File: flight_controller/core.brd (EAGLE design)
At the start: 94 x 90 mm, 116 parts, among them J1 MOLEX-2POS, J10 MOLEX-2POS, J11 MOLEX-2POS, J12 MOLEX-2POS, J13 MOLEX-3POS, J14 MOLEX-3POS, J15 MOLEX-4POS, J16 MOLEX-3POS, J17 MOLEX-3POS, J18 MOLEX-4POS, J19 MOLEX-3POS, J2 MOLEX-2POS, J20 MOLEX-4POS, J3 MOLEX-2POS, J4 MOLEX-2POS, J5 MOLEX-2POS, J6 MOLEX-2POS, J7 MOLEX-2POS, J8 MOLEX-2POS, J9 MOLEX-2POS, Q1 MMBT2222A, Q14 MMBT2222A, Q15 MMBT2222A, Q16 MMBT2222A, Q17 MMBT2222A, Q3 MMBT2222A, Q4 MMBT2222A, Q9 MMBT2222A, U1 MPU-6000QFN-24, U2 MEAS-MS5611, U3 USD-SOCKETNEW, U4 STM32F405, U5 MIC5219 3.3V

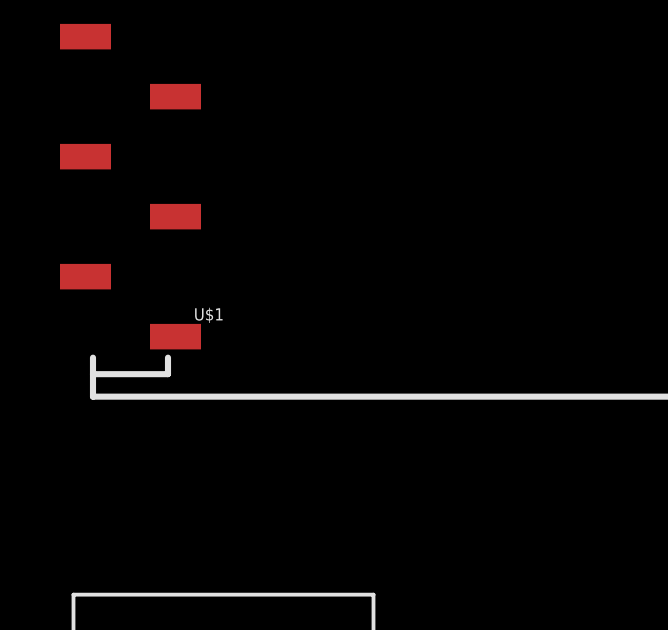
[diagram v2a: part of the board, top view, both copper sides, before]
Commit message: Explicitly name XBee package.
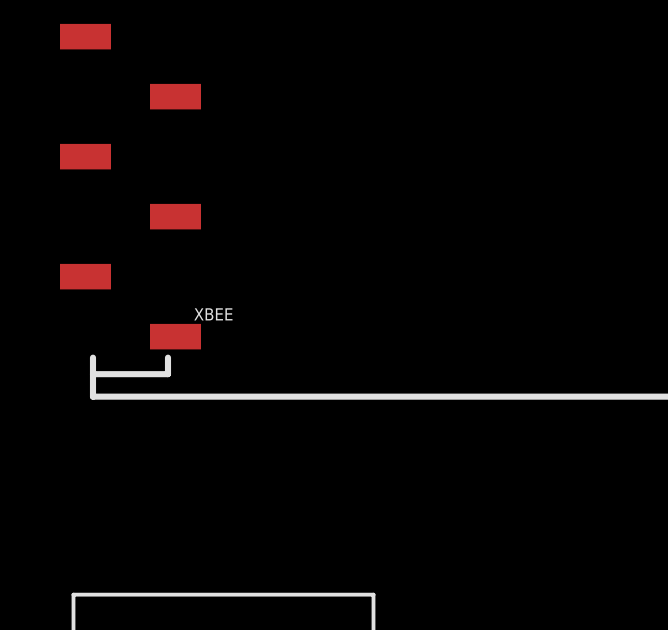
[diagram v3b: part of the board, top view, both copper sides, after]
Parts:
- renumbered U$1 to XBEE
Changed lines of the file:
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@@
 <attribute name="PROD_ID" value="CAP-08267" x="-187.5" y="-506.7" size="1.778" layer="27" display="off"/>
 </element>
-<element name="U$1" library="SparkFun-RF" package="XBEE-SMD" value="XBEE-1B3" x="-202.6" y="-501.9">
+<element name="XBEE" library="SparkFun-RF" package="XBEE-SMD" value="XBEE-1B3" x="-202.6" y="-501.9">
 <attribute name="PROD_ID" value="CONN-09042" x="-202.6" y="-501.9" size="1.778" layer="27" display="off"/>
 </element>
@@
 <contactref element="C15" pad="2"/>
 <contactref element="C16" pad="2"/>
-<contactref element="U$1" pad="10"/>
+<contactref element="XBEE" pad="10"/>
 <contactref element="J18" pad="4"/>
 <contactref element="R13" pad="1"/>
@@
 <contactref element="R8" pad="1"/>
 <contactref element="J20" pad="1"/>
-<contactref element="U$1" pad="5"/>
+<contactref element="XBEE" pad="5"/>
 <contactref element="U4" pad="7"/>
 <wire x1="-11.4" y1="-155.2" x2="-14.15" y2="-182.7" width="0" layer="19" extent="1-1"/>
@@
 <contactref element="U4" pad="64"/>
 <contactref element="C9" pad="1"/>
-<contactref element="U$1" pad="1"/>
+<contactref element="XBEE" pad="1"/>
 <wire x1="-138" y1="-372.6" x2="-129.4" y2="-372.6" width="0" layer="19" extent="1-1"/>
 <wire x1="-180.7138" y1="-413.9967" x2="-138" y2="-372.6" width="0" layer="19" extent="1-1"/>
@@
 <contactref element="R11" pad="1"/>
 <contactref element="R13" pad="2"/>
-<contactref element="U$1" pad="20"/>
+<contactref element="XBEE" pad="20"/>
 <wire x1="-184.75" y1="-435.8" x2="-27.55" y2="-219.5" width="0" layer="19" extent="1-1"/>
 <wire x1="-183.05" y1="-438.8" x2="-184.75" y2="-435.8" width="0" layer="19" extent="1-1"/>
@@
 <signal name="RSSI">
 <contactref element="R27" pad="1"/>
-<contactref element="U$1" pad="6"/>
+<contactref element="XBEE" pad="6"/>
 <wire x1="-212.1" y1="-491.9" x2="-30.65" y2="-219.5" width="0" layer="19" extent="1-1"/>
 </signal>
@@
 <signal name="UART2-TX-XBEE">
 <contactref element="U4" pad="16"/>
-<contactref element="U$1" pad="3"/>
+<contactref element="XBEE" pad="3"/>
 <contactref element="J17" pad="1"/>
 <contactref element="R29" pad="1"/>
@@
 <signal name="UART2-RX-XBEE">
 <contactref element="U4" pad="17"/>
-<contactref element="U$1" pad="2"/>
+<contactref element="XBEE" pad="2"/>
 <contactref element="J17" pad="2"/>
 <contactref element="R30" pad="1"/>

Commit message: Remove XBee reset pin from global reset net.
The XBee pin is for factory resetting the device! Read the datasheet, people!
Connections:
- net RST: no longer XBEE.5
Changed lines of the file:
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@@
 <contactref element="R8" pad="1"/>
 <contactref element="J20" pad="1"/>
-<contactref element="XBEE" pad="5"/>
 <contactref element="U4" pad="7"/>
 <wire x1="-11.4" y1="-155.2" x2="-14.15" y2="-182.7" width="0" layer="19" extent="1-1"/>
 <wire x1="-42.794" y1="-359.895" x2="-14.15" y2="-182.7" width="0" layer="19" extent="1-1"/>
 <wire x1="-183" y1="-382.5" x2="-42.794" y2="-359.895" width="0" layer="19" extent="1-1"/>
-<wire x1="-215.1" y1="-489.9" x2="-183" y2="-382.5" width="0" layer="19" extent="1-1"/>
 </signal>
 <signal name="PA12">

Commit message: Add RGB status LED pair.
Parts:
- removed J10, J11, J12: MOLEX-2POS, aerial:MOLEX-2MM-MICROLATCH-2POS-RA
- removed LED16, LED17, LED18, LED19, LED20, LED21: GREEN, SparkFun-LED:LED-0603
- removed R35, R36: 680, SparkFun-Passives:0603-RES
- added Q2, Q5, Q6: 200mA/50V, SparkFun-DiscreteSemi:SOT23-3
- LED14, LED15: value GREEN -> OSRAM-MULTILED-RGB; device SparkFun-LED:LED-0603 -> aerial:PLCC-6
- R10, R26: value 680 -> 120
- R24, R25, R33, R34: value 680 -> 100
- moved R34 388.2 mm to (-223.8, -555.1)
- moved R33 384.0 mm to (-223.8, -552.1)
- moved R24 383.1 mm to (-223.8, -543.1)
- moved R26 380.9 mm to (-223.8, -549.1)
- moved R25 376.7 mm to (-223.8, -546.1)
- moved LED15 376.2 mm to (-222.5, -537.0)
- moved LED5 365.7 mm to (-214.8, -519.7)
- moved LED6 365.7 mm to (-211.9, -519.7)
- moved LED14 365.1 mm to (-213.3, -531.3)
- moved LED7 359.8 mm to (-214.8, -522.8)
- moved R10 247.7 mm to (-223.8, -540.1)
- moved R4 233.2 mm to (-214.5, -525.7)
- moved R3 226.7 mm to (-211.6, -522.6)
- moved R7 226.6 mm to (-211.4, -525.7)
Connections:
- net TIM3-CH1-K renamed TIM4-CH1-K
- net TIM3-CH2-K renamed TIM4-CH2-K
- net TIM3-CH3-K renamed TIM4-CH3-K
- net TIM3-CH4-K renamed TIM4-CH4-K
- removed net N$31: LED5.A, R24.2
- removed net N$32: LED6.A, R25.2
- removed net N$33: LED7.A, R26.2
- removed net N$40: LED14.A, R33.2
- removed net N$41: LED15.A, R34.2
- removed net N$42: LED16.A, R35.2
- removed net N$43: LED17.A, R36.2
- removed net RSSI: R27.1, XBEE.6
- removed net TIM3-CH2: R10.1, R40.1, U4.23
- removed net TIM3-CH3: R3.1, R41.1, U4.26
- removed net TIM3-CH4: R4.1, R42.1, U4.27
- new net N$12: LED14.A1, R25.2
- new net N$19: LED15.A1, R34.2
- new net N$3: LED6.A, R4.2
- new net N$5: LED14.C1, LED15.C1, Q2.3
- new net N$6: LED14.C3, LED15.C3, Q5.3
- new net N$7: LED14.C2, LED15.C2, Q6.3
- new net N$8: LED14.A2, R10.2
- new net N$9: LED14.A3, R24.2
- new net TIM3-CH1-RSSI: R27.1, U4.22, XBEE.6
- new net TIM3-CH2-STSB: Q2.1
- new net TIM3-CH2-STSR: U4.23
- new net TIM3-CH3-STSG: Q5.1, U4.26
- new net TIM3-CH4-STSB: U4.27
- new net TIM3-CH4-STSR: Q6.1
- net 5V: now also R10.1, R24.1, R25.1, R26.1, R33.1, R34.1
- net GND: now also Q2.2, Q5.2, Q6.2; no longer J10.2, J11.2, J12.2, LED14.C, LED15.C, LED16.C, LED17.C, LED18.C, LED19.C, LED20.C, LED21.C
- net N$15: now also LED15.A2, R26.2; no longer LED20.A, R7.2
- net N$16: now also LED15.A3, R33.2; no longer LED21.A, R10.2
- net N$2: now also LED5.A; no longer LED18.A
- net N$4: now also LED7.A, R7.2; no longer LED19.A, R4.2
- net PA12: now also R3.1; no longer R25.1
- net PA15: now also R4.1; no longer R26.1
- net PB2: now also R7.1; no longer R24.1
- net TIM1-CH1: no longer R35.1
- net TIM1-CH2: no longer R36.1
- net TIM1-CH3: no longer R33.1
- net TIM1-CH4: no longer R34.1
- net TIM3-CH1: now also J9.1; no longer R39.1, R7.1, U4.22
- net TIM4-CH1: now also R39.1; no longer J9.1
- net TIM4-CH2: now also R40.1; no longer J10.1
- net TIM4-CH3: now also R41.1; no longer J11.1
- net TIM4-CH4: now also R42.1; no longer J12.1

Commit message: Replace components to those from new OSURC libraries.
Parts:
- J1: device aerial:MOLEX-2MM-MICROLATCH-2POS-RA -> OSURC_Connectors:MOLEX-2MM-MICROLATCH-2POS-RA
- J17: device aerial:MOLEX-2MM-MICROLATCH-3POS-RA -> OSURC_Connectors:MOLEX-2MM-MICROLATCH-3POS-RA
- J18: device aerial:MOLEX-2MM-MICROLATCH-4POS-RA -> OSURC_Connectors:MOLEX-2MM-MICROLATCH-4POS-RA
- LED14: device aerial:PLCC-6 -> OSURC_LED:PLCC-6
- U2: device aerial:MEAS-MS5611 -> OSURC_Sensors:MEAS-MS5611
- U4: device aerial:LQFP-64-STM32F405 -> OSURC_DigitalIC:LQFP-64-STM32F405
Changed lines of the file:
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@@
 <attribute name="PROD_ID" value="CONN-07820" x="-0.5" y="-145.6" size="1.778" layer="27" display="off"/>
 </element>
-<element name="U4" library="aerial" package="LQFP-64-STM32F405" value="STM32F405" x="-11.8" y="-162.3"/>
+<element name="U4" library="OSURC_DigitalIC" package="LQFP-64-STM32F405" value="STM32F405" x="-11.8" y="-162.3"/>
 <element name="R8" library="SparkFun" package="0603-RES" value="20K" x="-13.3" y="-182.7"/>
 <element name="C8" library="SparkFun-Capacitors" package="0603-CAP" value="0.1uF" x="-20.4" y="-191.9">
@@
 <attribute name="PROD_ID" value="SWCH-08247" x="-40" y="-361.8" size="1.778" layer="27" display="off"/>
 </element>
-<element name="J1" library="aerial" package="MOLEX-2MM-MICROLATCH-2POS-RA" value="MOLEX-2POS" x="-48" y="-372.6"/>
+<element name="J1" library="OSURC_Connectors" package="MOLEX-2MM-MICROLATCH-2POS-RA" value="MOLEX-2POS" x="-48" y="-372.6"/>
 <element name="J2" library="aerial" package="MOLEX-2MM-MICROLATCH-2POS-RA" value="MOLEX-2POS" x="-54.8" y="-372.6"/>
 <element name="J3" library="aerial" package="MOLEX-2MM-MICROLATCH-2POS-RA" value="MOLEX-2POS" x="-61.6" y="-372.6"/>
@@
 <element name="J14" library="aerial" package="MOLEX-2MM-MICROLATCH-3POS-RA" value="MOLEX-3POS" x="-140" y="-372.6"/>
 <element name="J16" library="aerial" package="MOLEX-2MM-MICROLATCH-3POS-RA" value="MOLEX-3POS" x="-157.2" y="-372.6"/>
-<element name="J17" library="aerial" package="MOLEX-2MM-MICROLATCH-3POS-RA" value="MOLEX-3POS" x="-165.8" y="-372.6"/>
+<element name="J17" library="OSURC_Connectors" package="MOLEX-2MM-MICROLATCH-3POS-RA" value="MOLEX-3POS" x="-165.8" y="-372.6"/>
 <element name="J19" library="aerial" package="MOLEX-2MM-MICROLATCH-3POS-RA" value="MOLEX-3POS" x="-183" y="-372.6"/>
 <element name="J20" library="aerial" package="MOLEX-2MM-MICROLATCH-4POS-RA" value="MOLEX-4POS" x="-183" y="-382.5"/>
@@
 <attribute name="PROD_ID" value="CAP-07888" x="-183.9" y="-463.4" size="1.778" layer="27" display="off"/>
 </element>
-<element name="U2" library="aerial" package="MEAS-MS5611" value="MEAS-MS5611" x="-187.3" y="-462.4"/>
+<element name="U2" library="OSURC_Sensors" package="MEAS-MS5611" value="MEAS-MS5611" x="-187.3" y="-462.4"/>
 <element name="C14" library="SparkFun-Capacitors" package="0603-CAP" value="0.1uF" x="-187.5" y="-466.4">
 <attribute name="PROD_ID" value="CAP-08604" x="-187.5" y="-466.4" size="1.778" layer="27" display="off"/>
@@
 <attribute name="PROD_ID" value="CONN-09042" x="-202.6" y="-501.9" size="1.778" layer="27" display="off"/>
 </element>
-<element name="J18" library="aerial" package="MOLEX-2MM-MICROLATCH-4POS-RA" value="MOLEX-4POS" x="-213.5" y="-514.2"/>
+<element name="J18" library="OSURC_Connectors" package="MOLEX-2MM-MICROLATCH-4POS-RA" value="MOLEX-4POS" x="-213.5" y="-514.2"/>
 <element name="R3" library="SparkFun-Passives" package="0603-RES" value="680" x="-211.6" y="-522.6"/>
 <element name="R4" library="SparkFun-Passives" package="0603-RES" value="680" x="-214.5" y="-525.7"/>
@@
 <element name="LED6" library="SparkFun-LED" package="LED-0603" value="ORANGE" x="-211.9" y="-519.7"/>
 <element name="LED7" library="SparkFun-LED" package="LED-0603" value="ORANGE" x="-214.8" y="-522.8"/>
-<element name="LED14" library="aerial" package="PLCC-6" value="OSRAM-MULTILED-RGB" x="-213.3" y="-531.3"/>
+<element name="LED14" library="OSURC_LED" package="PLCC-6" value="OSRAM-MULTILED-RGB" x="-213.3" y="-531.3"/>
 <element name="Q2" library="SparkFun-DiscreteSemi" package="SOT23-3" value="200mA/50V" x="-217.6" y="-531.4">
 <attribute name="PROD_ID" value="TRANS-00830" x="-217.6" y="-531.4" size="1.778" layer="27" display="off"/>

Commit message: Change kill BJTs to dual N-ch MOSFETs.
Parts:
- removed Q1, Q14, Q15, Q16, Q17, Q3, Q4, Q9: MMBT2222A, SparkFun-DiscreteSemi:SOT23-3
- removed R11, R12, R13, R19, R20, R23, R39, R40, R41, R42: 1K, SparkFun:0603-RES
- added Q10, Q11, Q7, Q8: EM6K1, OSURC_DiscreteSemi:SOT-666
- added R35, R36, R38, R43, R44, R45, R46, R47, R48: 1K, SparkFun:0603-RES
- J1: value MOLEX-2POS -> M02
- J17: value MOLEX-3POS -> M03
- J18: value MOLEX-4POS -> M04
- LED15: device aerial:PLCC-6 -> OSURC_LED:PLCC-6
- Y1: value (none) -> 16MHz
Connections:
- removed net KILL-BASE: Q1.1, Q14.1, Q15.1, Q16.1, Q17.1, Q3.1, Q4.1, Q9.1, R11.2
- new net KILL1: Q10.2, Q10.5, Q11.2, Q11.5
- net 3.3V: now also R48.2
- net GND: now also Q10.1, Q10.4, Q11.1, Q11.4, Q7.1, Q7.4, Q8.1, Q8.4; no longer Q1.2, Q14.2, Q15.2, Q16.2, Q17.2, Q3.2, Q4.2, Q9.2, R13.1
- net KILL: now also Q7.2, Q7.5, Q8.2, Q8.5, R48.1; no longer R11.1, R13.2
- net TIM1-CH1: now also R35.2; no longer R12.1
- net TIM1-CH1-K: now also Q7.6, R35.1; no longer Q1.3, R12.2
- net TIM1-CH2: now also R36.2; no longer R19.1
- net TIM1-CH2-K: now also Q7.3, R36.1; no longer Q3.3, R19.2
- net TIM1-CH3: now also R38.2; no longer R20.1
- net TIM1-CH3-K: now also Q8.6, R38.1; no longer Q4.3, R20.2
- net TIM1-CH4: now also R43.2; no longer R23.1
- net TIM1-CH4-K: now also Q8.3, R43.1; no longer Q9.3, R23.2
- net TIM4-CH1: now also R44.2; no longer R39.1
- net TIM4-CH1-K: now also Q10.6, R44.1; no longer Q14.3, R39.2
- net TIM4-CH2: now also R45.2; no longer R40.1
- net TIM4-CH2-K: now also Q10.3, R45.1; no longer Q15.3, R40.2
- net TIM4-CH3: now also R46.2; no longer R41.1
- net TIM4-CH3-K: now also Q11.6, R46.1; no longer Q16.3, R41.2
- net TIM4-CH4: now also R47.2; no longer R42.1
- net TIM4-CH4-K: now also Q11.3, R47.1; no longer Q17.3, R42.2
